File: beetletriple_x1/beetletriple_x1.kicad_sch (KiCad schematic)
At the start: 1 part, among them J1 Power IN

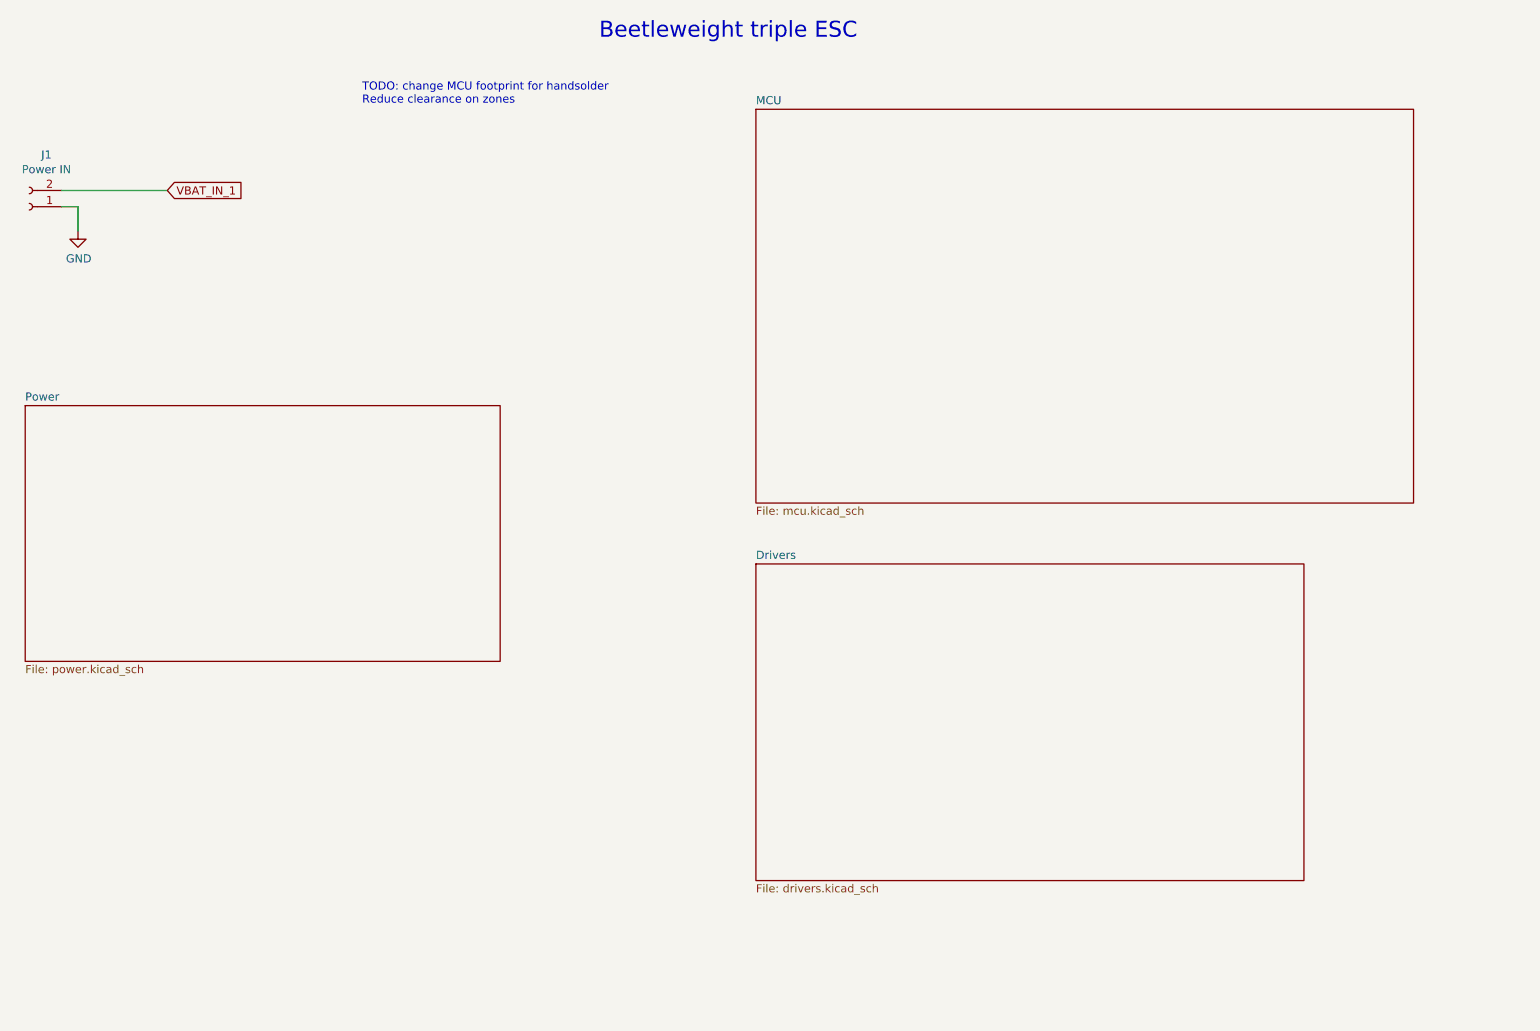
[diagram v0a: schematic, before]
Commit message: Add gate resistors; re-layout
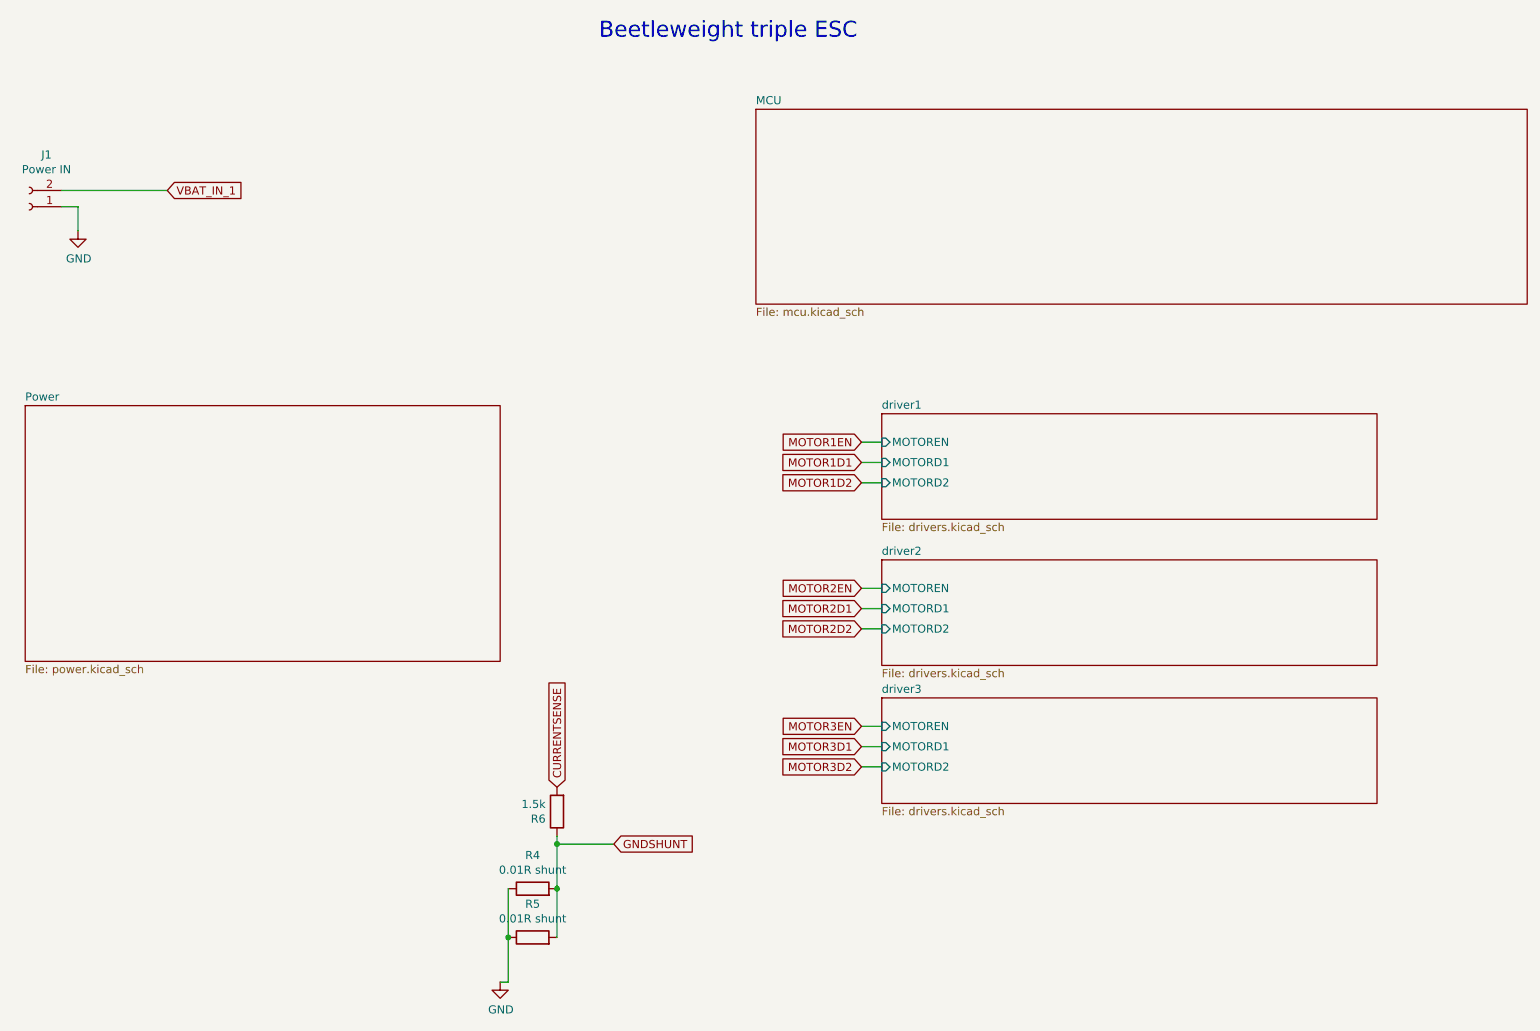
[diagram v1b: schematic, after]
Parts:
- added R4, R5: 0.01R shunt, Resistor_SMD:R_2512_6332Metric_Pad1.40x3.35mm_HandSolder, symbol Device:R
- added R6: 1.5k, Resistor_SMD:R_0805_2012Metric, symbol Device:R
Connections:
- net GND: now also R4.1, R5.1
- new net CURRENTSENSE: R6.2
- new net GNDSHUNT: R4.2, R5.2, R6.1
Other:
- sheet Drivers renamed driver1
- added sheet driver2 (drivers.kicad_sch)
- added sheet driver3 (drivers.kicad_sch)
- sheet driver1 ports: added MOTORD1, MOTORD2, MOTOREN; removed none
- note removed: "TODO: change MCU footprint for handsolder Reduce clearance on zones"

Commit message: Footprints shenanigans
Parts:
- added TP3, TP4: TestPoint, TestPoint:TestPoint_Pad_1.5x1.5mm, symbol Connector:TestPoint
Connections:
- new net driver1/TESTH1: TP4.1
- new net driver1/TESTL1: TP3.1
- no-connect marks 0 -> 4
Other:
- sheet driver1 ports: added TESTH1, TESTL1; removed none
- sheet driver2 ports: added TESTH1, TESTL1; removed none
- sheet driver3 ports: added TESTH1, TESTL1; removed none
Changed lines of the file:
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@@
   (junction (at 107.315 155.575) (diameter 0.9144) (color 0 0 0 0))
   (junction (at 107.315 162.56) (diameter 0.9144) (color 0 0 0 0))
+  (no_connect (at 184.785 111.125))
+  (no_connect (at 184.785 132.715))
+  (no_connect (at 189.23 111.125))
+  (no_connect (at 189.865 132.715))
   (wire (pts (xy 29.845 53.34) (xy 46.355 53.34))
     (stroke (width 0) (type solid) (color 0 0 0 0))
@@
   )
   (wire (pts (xy 154.94 143.51) (xy 158.115 143.51))
+    (stroke (width 0) (type solid) (color 0 0 0 0))
+  )
+  (wire (pts (xy 180.975 84.455) (xy 180.975 88.265))
+    (stroke (width 0) (type solid) (color 0 0 0 0))
+  )
+  (wire (pts (xy 186.055 78.74) (xy 186.055 88.265))
     (stroke (width 0) (type solid) (color 0 0 0 0))
   )
@@
       (effects (font (size 1.27 1.27)) (justify right) hide)
     )
+  )
+  (symbol (lib_id "Connector:TestPoint") (at 180.975 84.455 0) (unit 1)
+    (in_bom yes) (on_board yes)
+    (property "Reference" "TP3" (id 0) (at 182.3721 81.4641 0)
+      (effects (font (size 1.27 1.27)) (justify left))
+    )
+    (property "Value" "TestPoint" (id 1) (at 182.3721 83.7628 0)
+      (effects (font (size 1.27 1.27)) (justify left))
+    )
+    (property "Footprint" "TestPoint:TestPoint_Pad_1.5x1.5mm" (id 2) (at 186.055 84.455 0)
+      (effects (font (size 1.27 1.27)) hide)
+    )
+    (property "Datasheet" "~" (id 3) (at 186.055 84.455 0)
+      (effects (font (size 1.27 1.27)) hide)
+    )
+    (pin "1")
+  )
+  (symbol (lib_id "Connector:TestPoint") (at 186.055 78.74 0) (unit 1)
+    (in_bom yes) (on_board yes)
+    (property "Reference" "TP4" (id 0) (at 187.4521 75.7491 0)
+      (effects (font (size 1.27 1.27)) (justify left))
+    )
+    (property "Value" "TestPoint" (id 1) (at 187.4521 78.0478 0)
+      (effects (font (size 1.27 1.27)) (justify left))
+    )
+    (property "Footprint" "TestPoint:TestPoint_Pad_1.5x1.5mm" (id 2) (at 191.135 78.74 0)
+      (effects (font (size 1.27 1.27)) hide)
+    )
+    (property "Datasheet" "~" (id 3) (at 191.135 78.74 0)
+      (effects (font (size 1.27 1.27)) hide)
+    )
+    (pin "1")
   )
   (symbol (lib_id "power:GND") (at 32.385 59.69 0) (unit 1)
@@
       (effects (font (size 1.27 1.27)) (justify left))
     )
+    (pin "TESTL1" input (at 180.975 88.265 90)
+      (effects (font (size 1.27 1.27)) (justify right))
+    )
+    (pin "TESTH1" input (at 186.055 88.265 90)
+      (effects (font (size 1.27 1.27)) (justify right))
+    )
   )
   (sheet (at 158.115 111.125) (size 77.47 16.51)
@@
       (effects (font (size 1.27 1.27)) (justify left))
     )
+    (pin "TESTH1" input (at 184.785 111.125 90)
+      (effects (font (size 1.27 1.27)) (justify right))
+    )
+    (pin "TESTL1" input (at 189.23 111.125 90)
+      (effects (font (size 1.27 1.27)) (justify right))
+    )
   )
   (sheet (at 158.115 132.715) (size 77.47 16.51)
@@
     (pin "MOTORD1" input (at 158.115 140.335 180)
       (effects (font (size 1.27 1.27)) (justify left))
+    )
+    (pin "TESTH1" input (at 184.785 132.715 90)
+      (effects (font (size 1.27 1.27)) (justify right))
+    )
+    (pin "TESTL1" input (at 189.865 132.715 90)
+      (effects (font (size 1.27 1.27)) (justify right))
     )
   )
@@
       (reference "R6") (unit 1) (value "1.5k") (footprint "Resistor_SMD:R_0805_2012Metric")
     )
+    (path "/4836a614-d4f4-4914-b3cb-9f43ba402189"
+      (reference "TP3") (unit 1) (value "TestPoint") (footprint "TestPoint:TestPoint_Pad_1.5x1.5mm")
+    )
+    (path "/295ee500-c5ae-4540-a2a3-10677248b001"
+      (reference "TP4") (unit 1) (value "TestPoint") (footprint "TestPoint:TestPoint_Pad_1.5x1.5mm")
+    )
     (path "/6d93a432-011d-4d1d-9c43-a648615a7ea3/b538e895-f3c3-446e-9001-2df4142c87bf"
       (reference "#FLG01") (unit 1) (value "PWR_FLAG") (footprint "")
@@
       (reference "C22") (unit 1) (value "DNP") (footprint "Capacitor_SMD:C_1206_3216Metric")
     )
+    (path "/6d93a432-011d-4d1d-9c43-a648615a7ea3/6c81ed90-1aab-401b-accb-94af9d9d68a1"
+      (reference "C?") (unit 1) (value "10uF 50V") (footprint "Capacitor_SMD:C_1206_3216Metric")
+    )
     (path "/6d93a432-011d-4d1d-9c43-a648615a7ea3/f25ce49b-41d1-4aa9-8d87-86ed60ba4a42"
       (reference "D1") (unit 1) (value "B340A-13-F") (footprint "Diode_SMD:D_SMA_Handsoldering")
@@
     )
     (path "/359c4f89-e272-46e6-af92-d7488b619549/448811ca-761a-435c-b830-f8dc07e8a775"
-      (reference "U3") (unit 1) (value "ATtiny1617-M") (footprint "Package_DFN_QFN:QFN-24-1EP_4x4mm_P0.5mm_EP2.6x2.6mm")
+      (reference "U3") (unit 1) (value "ATtiny1617-M") (footprint "beetletriple:qfn24-hand1")
     )
     (path "/88009e22-8327-4e67-a142-0e1ef6c68b73/ca6c68b4-d34e-4247-848e-0a19a5c2f1f0"
@@
     )
     (path "/88009e22-8327-4e67-a142-0e1ef6c68b73/9555e271-0a4a-4b93-aaf1-cf94a3835016"
-      (reference "U11") (unit 1) (value "NCP81155MN") (footprint "Package_DFN_QFN:DFN-8-1EP_3x3mm_P0.5mm_EP1.66x2.38mm")
+      (reference "U11") (unit 1) (value "NCP81155MNTXG") (footprint "beetletriple:DFN-8-3x3mm_hand1")
     )
     (path "/88009e22-8327-4e67-a142-0e1ef6c68b73/f9a3fc1f-475d-4827-8ba2-ebf2b4334478"
-      (reference "U12") (unit 1) (value "NCP81155MN") (footprint "Package_DFN_QFN:DFN-8-1EP_3x3mm_P0.5mm_EP1.66x2.38mm")
+      (reference "U12") (unit 1) (value "NCP81155MNTXG") (footprint "beetletriple:DFN-8-3x3mm_hand1")
     )
     (path "/f360ad5b-e010-4926-8063-93bb34809c48/ca6c68b4-d34e-4247-848e-0a19a5c2f1f0"
@@
     )
     (path "/f360ad5b-e010-4926-8063-93bb34809c48/9555e271-0a4a-4b93-aaf1-cf94a3835016"
-      (reference "U5") (unit 1) (value "NCP81155MN") (footprint "Package_DFN_QFN:DFN-8-1EP_3x3mm_P0.5mm_EP1.66x2.38mm")
+      (reference "U5") (unit 1) (value "NCP81155MNTXG") (footprint "beetletriple:DFN-8-3x3mm_hand1")
     )
     (path "/f360ad5b-e010-4926-8063-93bb34809c48/f9a3fc1f-475d-4827-8ba2-ebf2b4334478"
-      (reference "U6") (unit 1) (value "NCP81155MN") (footprint "Package_DFN_QFN:DFN-8-1EP_3x3mm_P0.5mm_EP1.66x2.38mm")
+      (reference "U6") (unit 1) (value "NCP81155MNTXG") (footprint "beetletriple:DFN-8-3x3mm_hand1")
     )
     (path "/c41b8fde-16a1-40a3-b50f-93eb31d01ada/ca6c68b4-d34e-4247-848e-0a19a5c2f1f0"
@@
     )
     (path "/c41b8fde-16a1-40a3-b50f-93eb31d01ada/9555e271-0a4a-4b93-aaf1-cf94a3835016"
-      (reference "U7") (unit 1) (value "NCP81155MN") (footprint "Package_DFN_QFN:DFN-8-1EP_3x3mm_P0.5mm_EP1.66x2.38mm")
+      (reference "U7") (unit 1) (value "NCP81155MNTXG") (footprint "beetletriple:DFN-8-3x3mm_hand1")
     )
     (path "/c41b8fde-16a1-40a3-b50f-93eb31d01ada/f9a3fc1f-475d-4827-8ba2-ebf2b4334478"
-      (reference "U8") (unit 1) (value "NCP81155MN") (footprint "Package_DFN_QFN:DFN-8-1EP_3x3mm_P0.5mm_EP1.66x2.38mm")
-    )
-  )
+      (reference "U8") (unit 1) (value "NCP81155MNTXG") (footprint "beetletriple:DFN-8-3x3mm_hand1")
+    )
+  )
